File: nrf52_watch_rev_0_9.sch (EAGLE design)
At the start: 25 parts, among them IC1 HOLYIOT_18010, IC2 MX25R6435FM2IL0, IC4 MMA8652FCR1, J1 0528921033

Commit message: first draft of routing done
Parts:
- added PRG: NO_BOM, Inventas-Connectors:SWD_PROG_POGO
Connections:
- net ACC_INT1: now also IC1.P0.22
- net ACC_INT2: now also IC1.P0.18
- net BTN_BOTTOM: now also IC1.P0.04
- net BTN_MID: now also IC1.P0.21
- net BTN_TOP: now also IC1.P0.19
- net GND: now also PRG.GND
- net I2C_SCL: now also IC1.P1.00
- net I2C_SDA: now also IC1.P1.03
- net LCD_DISP: now also IC1.P0.12
- net LCD_POWER_CONTROL: now also IC1.P0.23
- net LCD_SCLK: now also IC1.P0.05
- net LCD_SCS: now also IC1.P1.09
- net LCD_SI: now also IC1.P0.07
- net QSPI_CS: now also IC1.P0.28
- net QSPI_SCLK: now also IC1.P0.30
- net QSPI_SIO0: now also IC1.P0.29
- net QSPI_SIO1: now also IC1.P0.02
- net QSPI_SIO2: now also IC1.P0.03
- net QSPI_SIO3: now also IC1.P0.31
- net SWDCLK: now also PRG.SWCLK
- net SWDIO: now also PRG.SWDIO
- net VDD: now also PRG.VDD
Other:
- moved on the sheet: B2, C11, C5, U$1

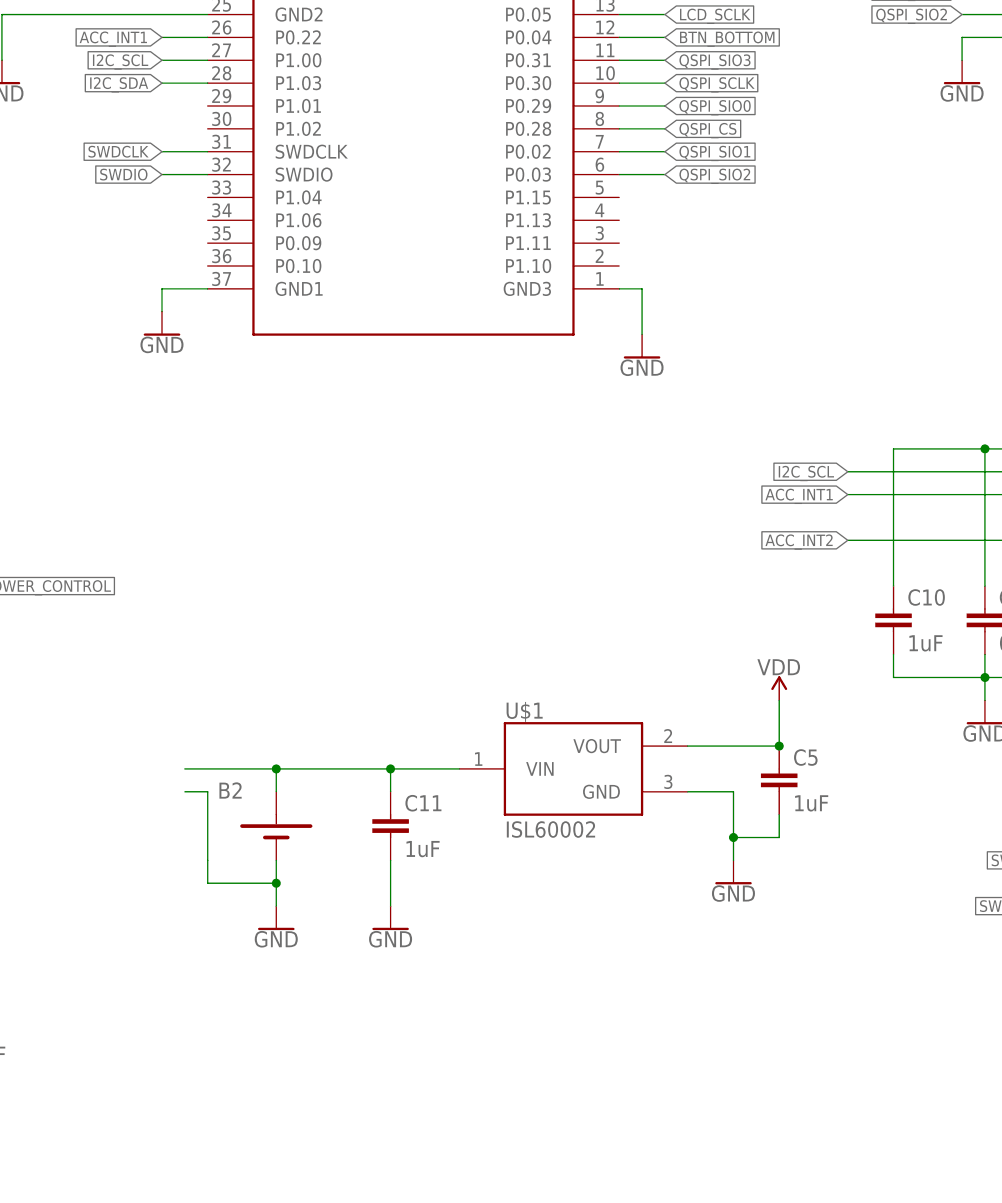
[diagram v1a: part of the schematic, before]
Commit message: changes to rouing. Added batter voltage measure. Added mounting holes
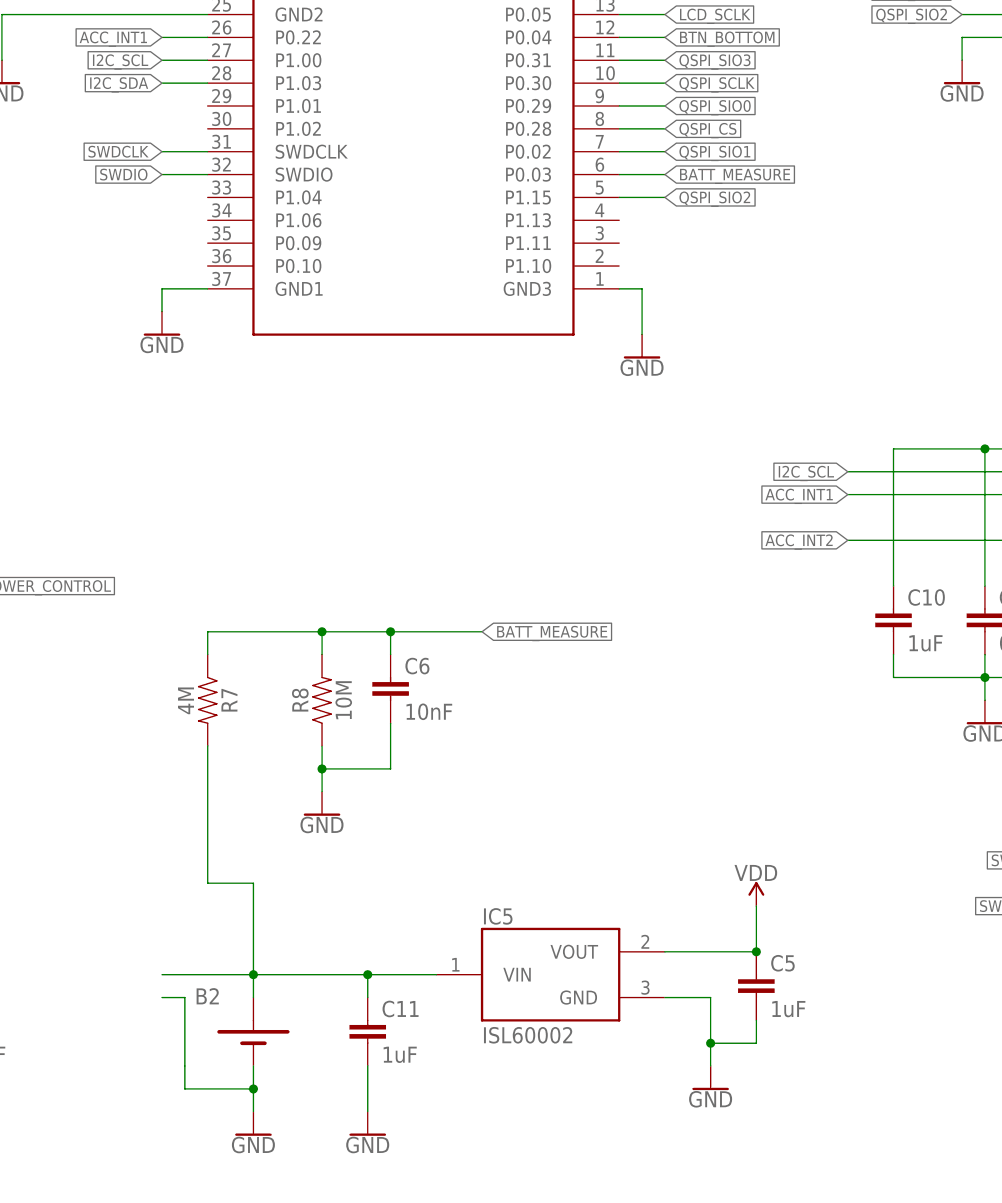
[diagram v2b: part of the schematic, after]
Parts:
- removed U$1: ISL60002, Inventas-Power:ISL60002
- added C6: 10nF, Inventas-Passives:CAP-6.3V-20%-0402
- added IC5: ISL60002, Inventas-Power:ISL60002
- added R7: 4M, Inventas-Passives:RES-0.063W-1%-0402
- added R8: 10M, Inventas-Passives:RES-0.063W-1%-0402
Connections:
- new net BATT_MEASURE: C6.1, IC1.P0.03, R7.1, R8.2
- net GND: now also C6.2, IC5.GND, R8.1; no longer U$1.GND
- net N$1: now also IC5.VIN, R7.2; no longer U$1.VIN
- net QSPI_SIO2: now also IC1.P1.15; no longer IC1.P0.03
- net VDD: now also IC5.VOUT; no longer U$1.VOUT
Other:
- moved on the sheet: B2, C11, C5

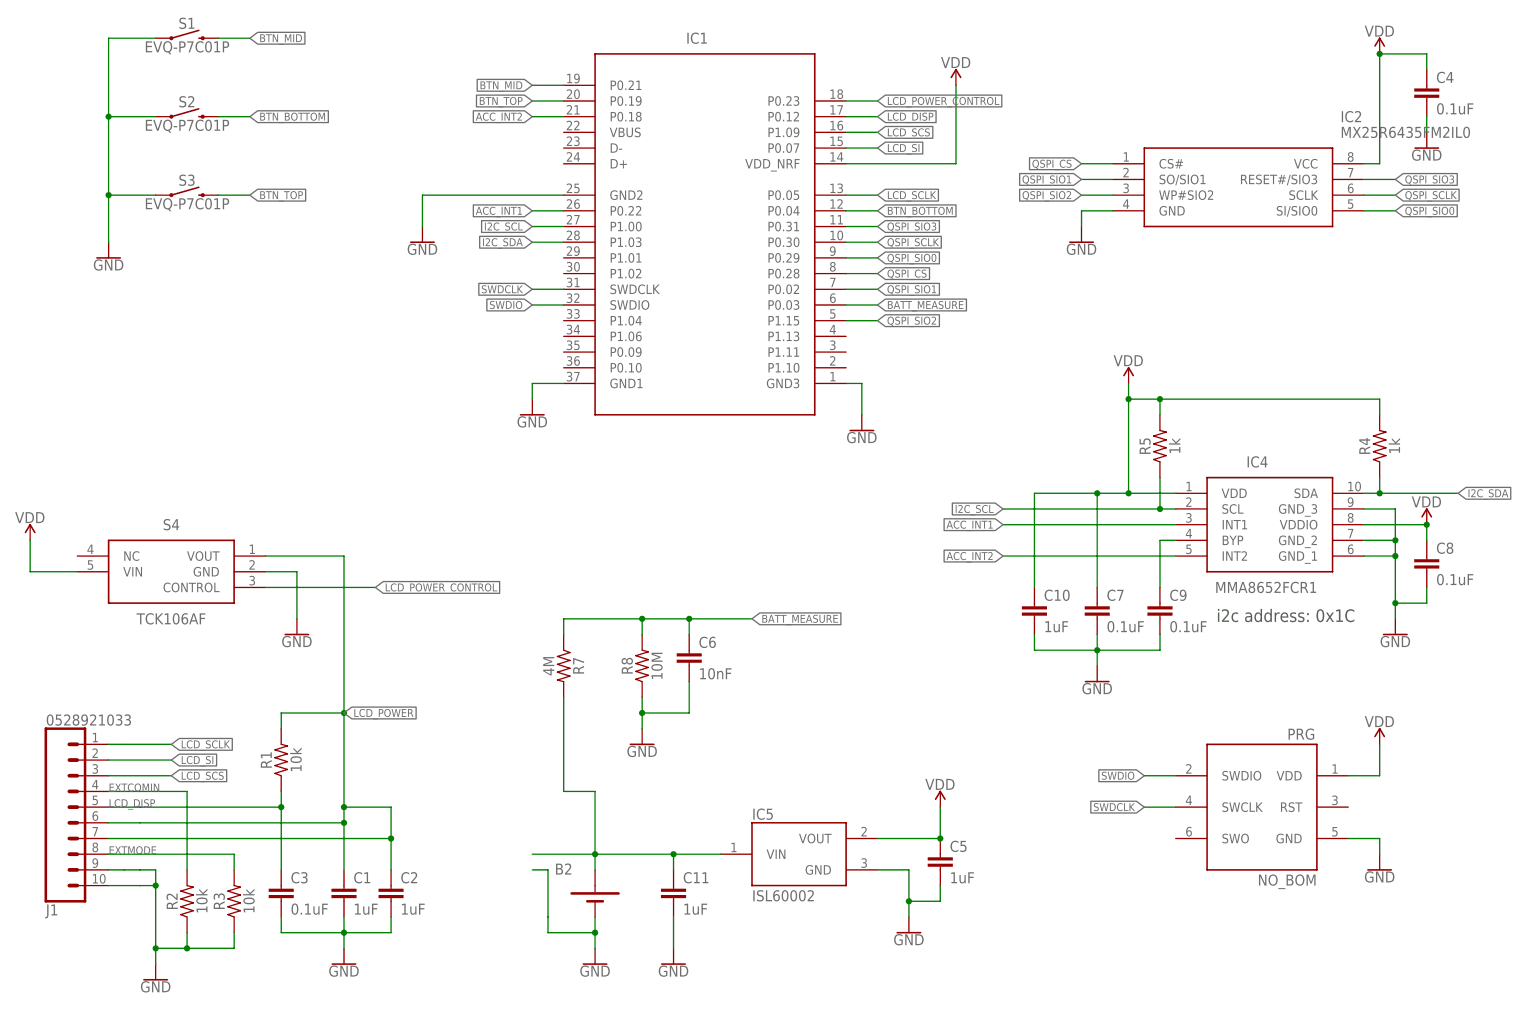
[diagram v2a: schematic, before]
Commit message: small fixes. all components are now 3D
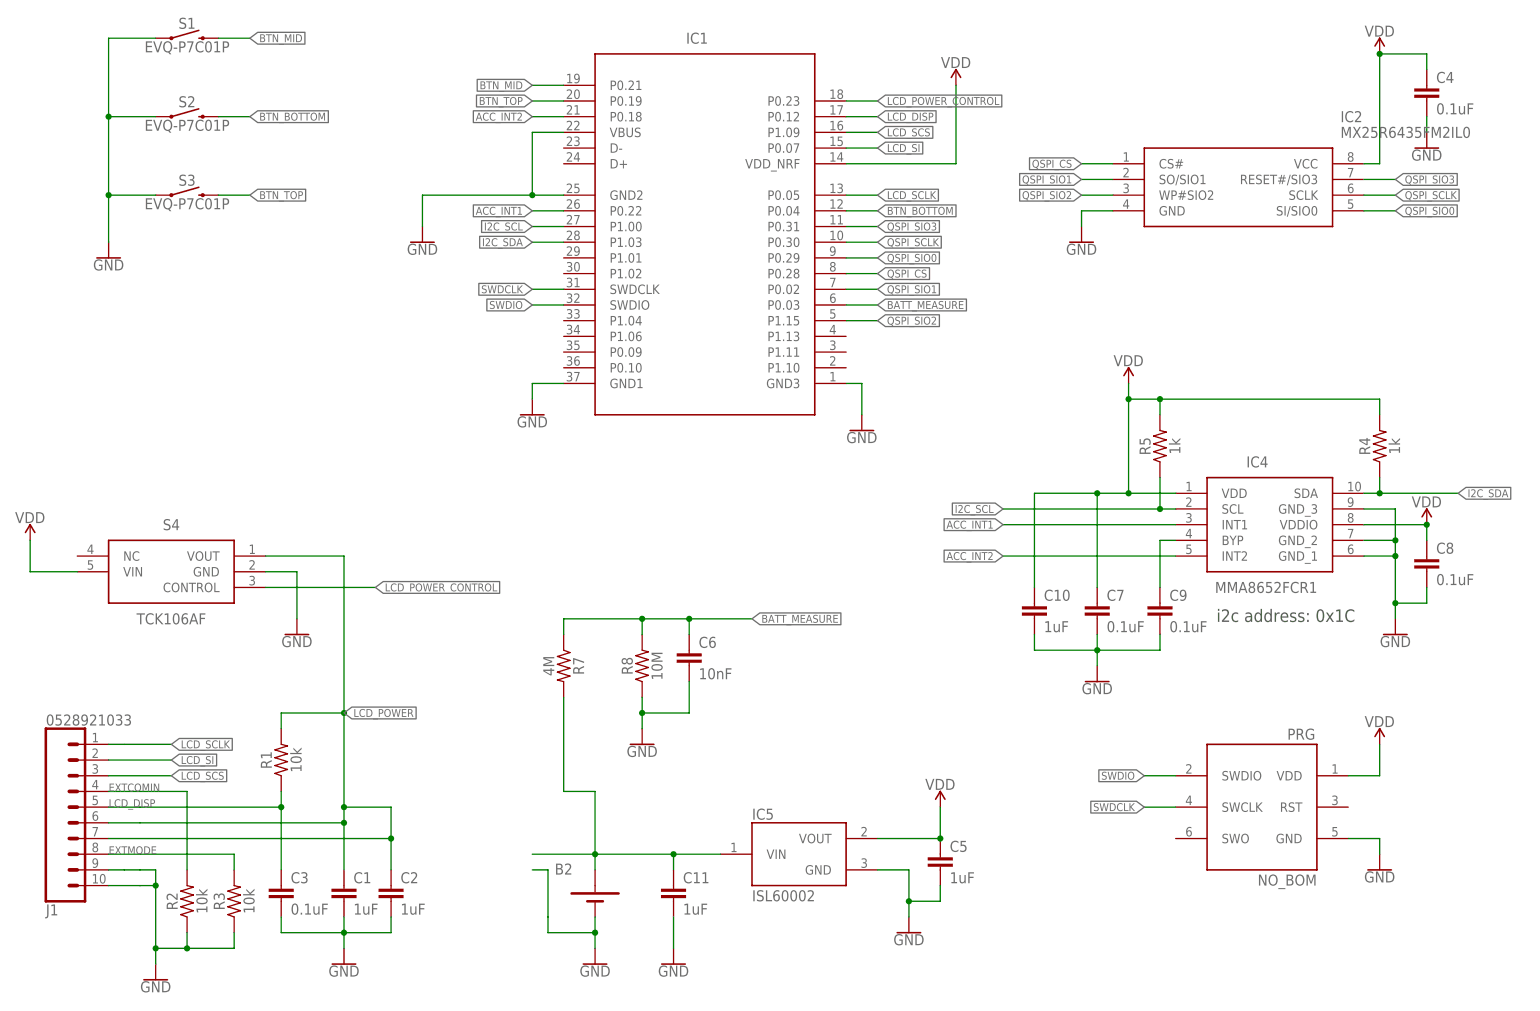
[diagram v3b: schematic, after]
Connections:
- net GND: now also IC1.VBUS
